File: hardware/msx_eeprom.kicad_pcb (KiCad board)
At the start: 2 copper layers, 99.8 x 64 mm, 96 parts, among them J1 Conn_02x07_Odd_Even, P1 MSX_CONNECTOR, U1 AT28C256-15PU

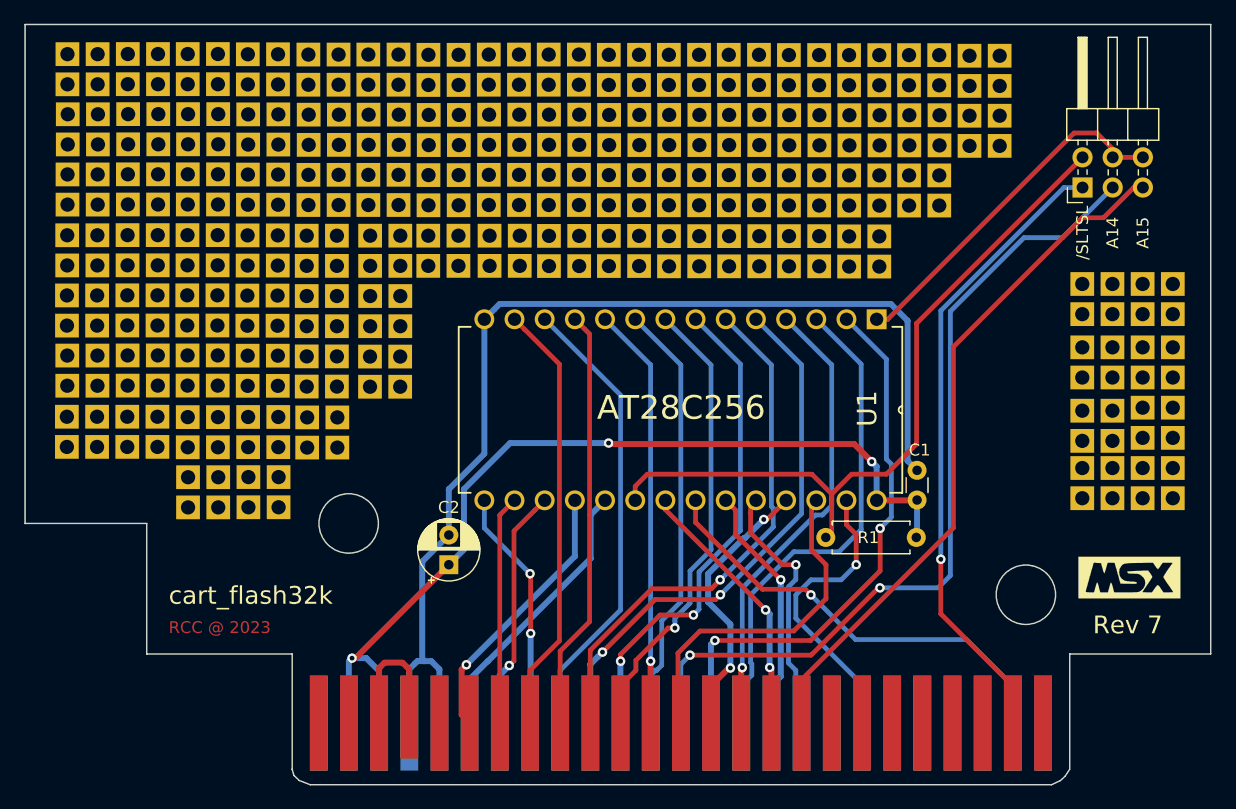
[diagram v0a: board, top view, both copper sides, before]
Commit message: Updated footprint to 2003 r1: pcb holes shiftted a little bit
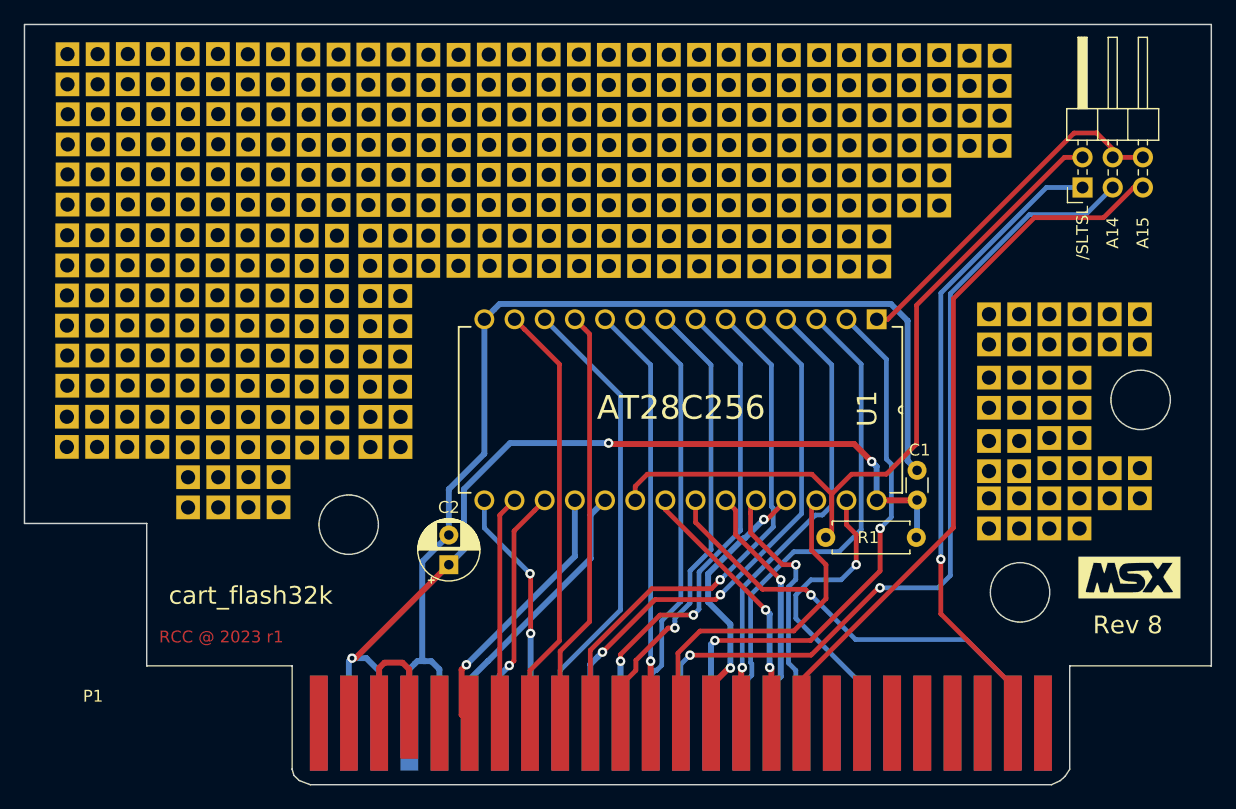
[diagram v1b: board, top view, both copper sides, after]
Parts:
- added _: _, Connector_Wire:SolderWirePad_2x02_P2.54mm_Drill0.8mm, F.Cu at (129.3, 52.6)
- added _: _, Connector_Wire:SolderWirePad_2x02_P2.54mm_Drill0.8mm, F.Cu at (139.4, 65.5)
- added _: _, Connector_Wire:SolderWirePad_2x02_P2.54mm_Drill0.8mm, F.Cu at (77.2, 61.2)
- P1: footprint Roni Footprints:MSX_CART_SW_Official -> Roni Footprints:MSX_CART_SW_Official_3Holes
- moved _ 8.26 mm to (129.3, 68.1)
- moved _ 8.26 mm to (134.4, 68.1)
- moved _ 8.26 mm to (134.4, 63.0)
- moved _ 8.26 mm to (134.4, 52.6)
- moved _ 8.26 mm to (134.4, 57.9)
- moved _ 8.26 mm to (129.3, 57.9)
- moved _ 8.26 mm to (129.3, 63.2)
- moved _ 3.44 mm to (139.4, 52.6)
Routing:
- net A15: track 61.6 -> 64.0 mm
- net mem_ce: track 61.5 -> 62.4 mm
- net A14: track 70.9 -> 71.8 mm
- net sltsl: track 56.6 -> 57.4 mm
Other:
- board size 99.8 x 64 mm -> 99.9 x 64 mm
- board text added: "Rev 8"
- board text removed: "Rev 7"

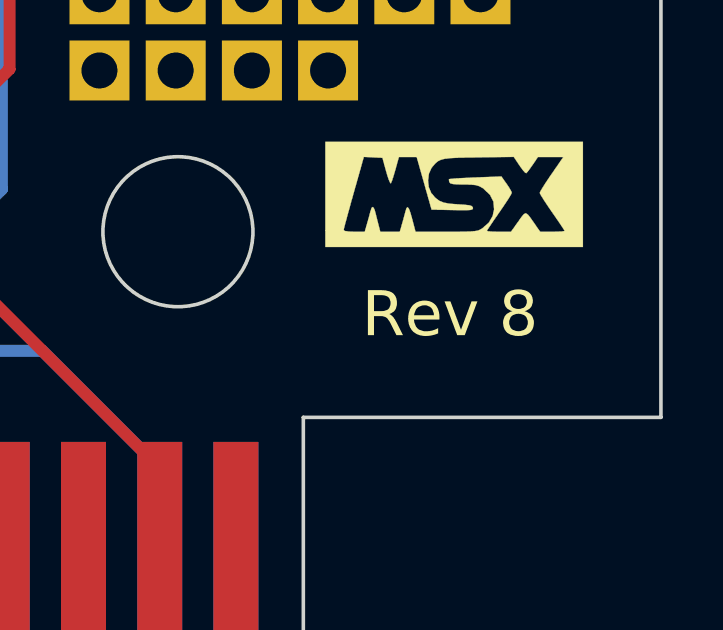
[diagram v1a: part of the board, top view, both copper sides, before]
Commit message: V8a - Added soldermask to edge area.
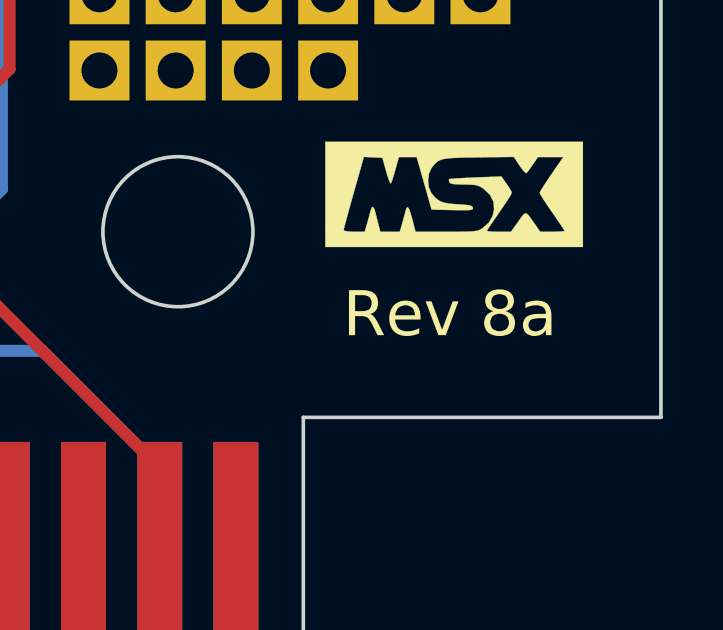
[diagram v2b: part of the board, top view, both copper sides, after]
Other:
- board text added: "Rev 8a"
- board text removed: "Rev 8"
